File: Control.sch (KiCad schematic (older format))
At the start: 27 parts, among them P15 USB_MINI, Q1 SMBT3904, Q2 SMBT3904, U3 CH340G, U4 ESP8266, Y1 Cristal

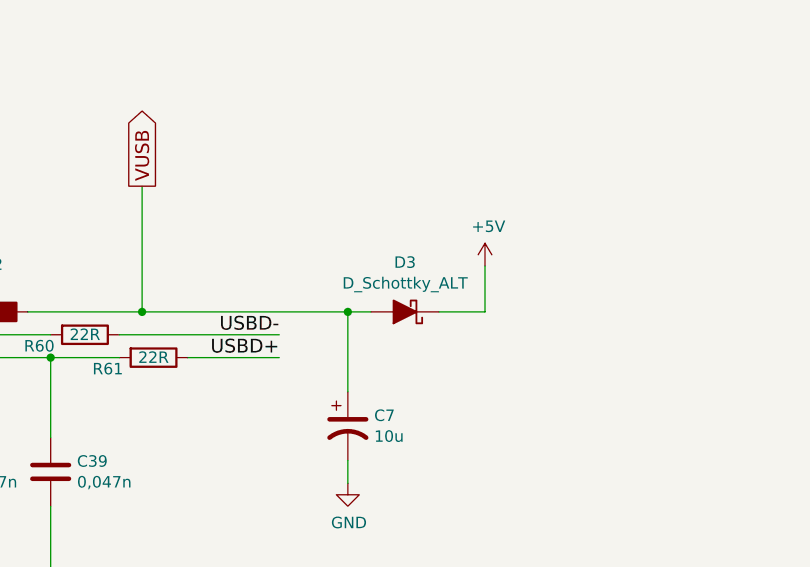
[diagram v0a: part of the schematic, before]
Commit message: añadidos valores y referencias a control, alimentacion y gpioEx
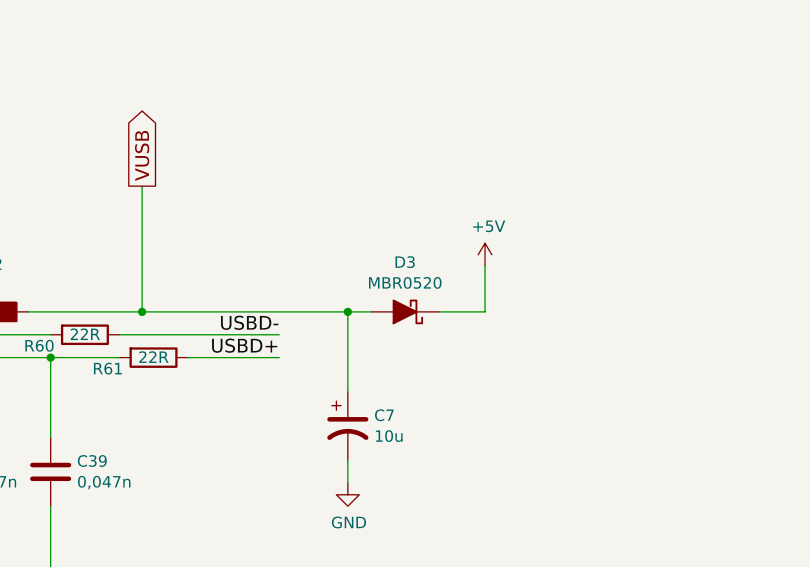
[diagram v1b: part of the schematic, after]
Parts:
- C10: Fabricante (none) -> SAMSUNG; Provedor (none) -> TME; Ref (none) -> CL21B471KBANNND; Ref_Proveedor (none) -> CL21B471KBANNND
- C11: Fabricante (none) -> SAMSUNG; Provedor (none) -> TME; Ref (none) -> CL31A107MQHNNNE; Ref_Proveedor (none) -> CL31A107MQHNNNE
- C38, C39: Fabricante (none) -> SAMSUNG; Provedor (none) -> TME; Ref (none) -> CL21C470JBANNNC; Ref_Proveedor (none) -> CL21C470JBANNNC
- C7: Fabricante (none) -> SAMSUNG; Provedor (none) -> TME; Ref (none) -> CL31B103KBCNNNC; Ref_Proveedor (none) -> CL31B103KBCNNNC
- C8, C9: Fabricante (none) -> SAMSUNG; Provedor (none) -> TME; Ref (none) -> CL21B104KBCNNNC; Ref_Proveedor (none) -> CL21B104KBCNNNC
- D3: value D_Schottky_ALT -> MBR0520; Fabricante (none) -> FAIRCHILD SEMICONDUCTOR; Provedor (none) -> tme; Ref (none) -> MBR0520L; Ref_Proveedor (none) -> MBR0520L
- F2: Fabricante (none) -> ece; Provedor (none) -> tme; Ref (none) -> SD050-16; Ref_Proveedor (none) -> SD050-16
- P15: Fabricante (none) -> MOLEX; Provedor (none) -> TME; Ref (none) -> 675031020; Ref_Proveedor (none) -> MX-67503-1020; Tolerancia (none) -> 1%
- R10, R11, R3, R4, R5, R6, R7: Fabricante (none) -> VISHAY; Potencia (none) -> 1/8W; Provedor (none) -> TME; Ref (none) -> CRCW080510K0FKEA; Ref_Proveedor (none) -> CRCW080510K0FKEA; Tolerancia (none) -> 1%
- R60, R61: Fabricante (none) -> VISHAY; Provedor (none) -> tme; Ref (none) -> CRCW080522R0FKEA; Ref_Proveedor (none) -> CRCW080522R0FKEA
- R8, R9: Fabricante (none) -> YAGEO; Provedor (none) -> TME; Ref (none) -> RC0805FR-07470RL; Ref_Proveedor (none) -> RC0805FR-07470R; Tolerancia (none) -> 1%
- U3: Provedor (none) -> aliexpres; Ref (none) -> CH340G

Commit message: actualizadas referencias en componentes y ordenado esquema electrico
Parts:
- C37: Fabricante (none) -> SAMSUNG; Provedor (none) -> tme; Ref (none) -> CL21B103JBANNNC; Ref_Proveedor (none) -> CL21B103JBANNNC
